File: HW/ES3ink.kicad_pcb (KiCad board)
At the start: 2 copper layers, 60.8 x 30 mm, 79 parts, among them J1 USB_C_Receptacle_USB2.0, J2 Conn_01x24_Pin, J3 Conn_01x02_Pin, J4 Conn_01x04_Socket, J5 USB_C_Receptacle_USB2.0, Q1 DMG3415U-7, Q2 SI1308EDL-T1-GE3, Q3 DMG3415U-7, Q4 SI2305, SW1 RESET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

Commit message: Version 2.5 upload
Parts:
- removed T1, T2, T3, T4: Tab, PCM_kikit:Tab
- removed kibuzzard-64559702: G***, kibuzzard-64559702
- added JP3: SolderJumper_2_Open, Jumper:SolderJumper-2_P1.3mm_Open_TrianglePad1.0x1.5mm, B.Cu at (42.1, -3.23)
- added kibuzzard-65023723: G***, kibuzzard-65023723, B.Cu at (3.00, -15.0)
- L1: value 68uH -> 10uH/1A
- R10: value 10R -> 2R2
- moved G*** 22.0 mm to (13.0, -15.0)
- moved G*** 20.0 mm to (32.5, -15.0)
- moved R3 18.4 mm to (19.2, -27.4), turned to 90 degrees
- moved C7 18.3 mm to (17.2, -27.4), turned to 90 degrees
- moved C22 12.5 mm to (37.9, -12.4), turned to -90 degrees
- moved R11 8.23 mm to (27.6, -12.4), turned to 90 degrees
- moved C13 8.18 mm to (29.7, -12.4), turned to 90 degrees
- moved Q2 7.70 mm to (38.7, -16.8), turned to -90 degrees
- moved C19 6.15 mm to (35.8, -16.9)
- moved L1 5.72 mm to (41.9, -12.6), turned to 0 degrees
- moved C14 4.50 mm to (35.8, -12.4), turned to -90 degrees
- moved R12 4.07 mm to (45.8, -12.4)
- moved D5 3.69 mm to (45.2, -16.9)
- moved Q3 3.60 mm to (42.2, -16.8)
- moved R10 3.46 mm to (41.9, -8.85)
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- renumbered C2 to C12.3546, R9 to R8.8456
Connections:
- Q1 pad 3: Net-(Q1-D) -> /3V3_EPD
- R10 pad 1: Net-(Q1-D) -> Net-(JP3-A)
- R10 pad 2: /3V3_EPD -> GND
- R8.8456 pad 2: GND -> Net-(JP3-A)
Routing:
- net /3V3_EPD: track 50.5 -> 18.9 mm, vias 3 -> 2
- net Net-(Q1-D): track 13.5 -> 0.00 mm
- net Net-(D1-A): track 32.3 -> 19.5 mm, vias 3 -> 0
- net /IO0: track 30.9 -> 20.0 mm, vias 0 -> 2
- net Net-(D5-K): track 77.6 -> 66.8 mm
- net Net-(D2-K): track 15.0 -> 5.21 mm, vias 2 -> 0
- net /GDR: track 15.9 -> 25.6 mm
- net /EN: track 43.4 -> 52.6 mm
- net Net-(JP3-A): track 0.00 -> 7.92 mm, vias 0 -> 1
- net /RESE: track 16.0 -> 23.5 mm
- net /IO48: track 26.4 -> 20.9 mm
- net GND: track 9.72 -> 4.67 mm, vias 20 -> 23
- net /IO8: track 13.7 -> 18.8 mm, vias 0 -> 2
- net /IO18: track 20.1 -> 15.1 mm, vias 2 -> 0
- net /P8: track 16.9 -> 21.6 mm, vias 0 -> 2
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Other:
- board text added: "R2.5"
- board text removed: "rev.Bi4"

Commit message: Layout change & production files
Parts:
- added G***: LOGO, LOGO, B.Cu at (44.3, -15.0)
- moved J4 21.7 mm to (24.5, -27.1)
- moved R6 21.4 mm to (25.7, -21.3)
- moved R7 21.3 mm to (23.7, -21.3)
- moved kibuzzard-64921EFB 19.1 mm to (47.6, -20.7)
- moved J3 19.0 mm to (44.2, -25.1)
- moved kibuzzard-64921EEB 18.9 mm to (40.8, -20.7)
- moved R20 13.3 mm to (29.6, -21.3), turned to -90 degrees
- moved C4 12.7 mm to (27.6, -21.3), turned to -90 degrees
- moved R19 9.38 mm to (31.6, -21.3), turned to -90 degrees
- moved R18 8.97 mm to (29.5, -28.3)
- moved D4 8.66 mm to (36.2, -21.3), turned to 90 degrees
- moved Q4 8.20 mm to (30.6, -24.8), turned to 180 degrees
- moved R15 5.41 mm to (38.5, -21.3)
- moved R17 4.66 mm to (38.5, -28.3)
- moved C5 4.57 mm to (47.8, -16.9), turned to 90 degrees
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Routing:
- net +5V: track 86.6 -> 60.2 mm
- net /IO4: track 65.2 -> 41.8 mm
- net /IO3: track 73.1 -> 49.7 mm
- net /BAT+: track 19.9 -> 35.0 mm, vias 0 -> 3
- net Net-(D4-K): track 2.02 -> 16.4 mm, vias 0 -> 2
- net /IO40: track 35.3 -> 21.0 mm
- net /IO2: track 44.1 -> 30.8 mm
- net +3V3: track 110.1 -> 121.4 mm, vias 5 -> 4
- net Net-(Q4-G): track 6.24 -> 12.8 mm, vias 0 -> 2
- net Net-(JP1-A): track 1.75 -> 5.40 mm
- net /GDR: track 25.6 -> 22.4 mm
- net Net-(JP2-A): track 1.75 -> 4.51 mm
- net GND: track 4.67 -> 6.65 mm, vias 23 -> 29
- net Net-(U3-STAT): track 2.81 -> 4.57 mm
- net /IO48: track 20.9 -> 19.2 mm
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
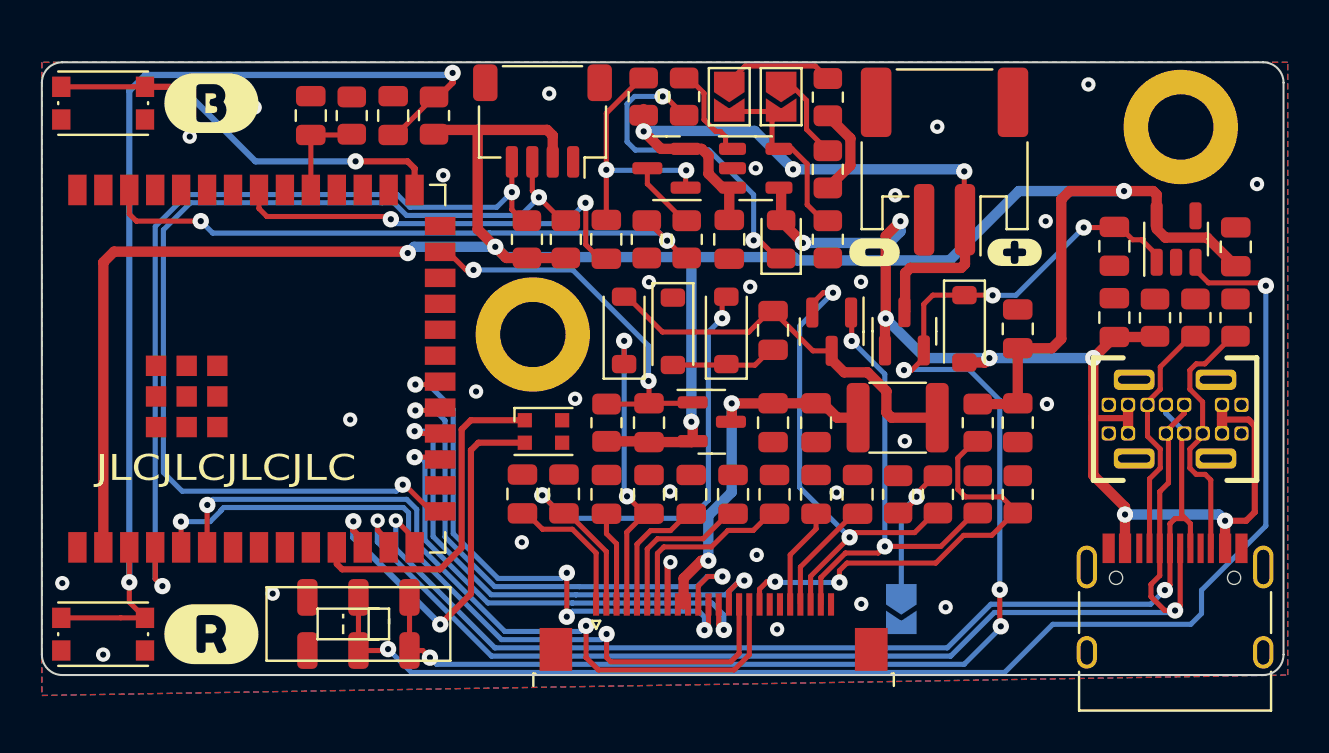
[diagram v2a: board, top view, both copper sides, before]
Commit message: PCB size increase so it can be manufactured with V-cuts
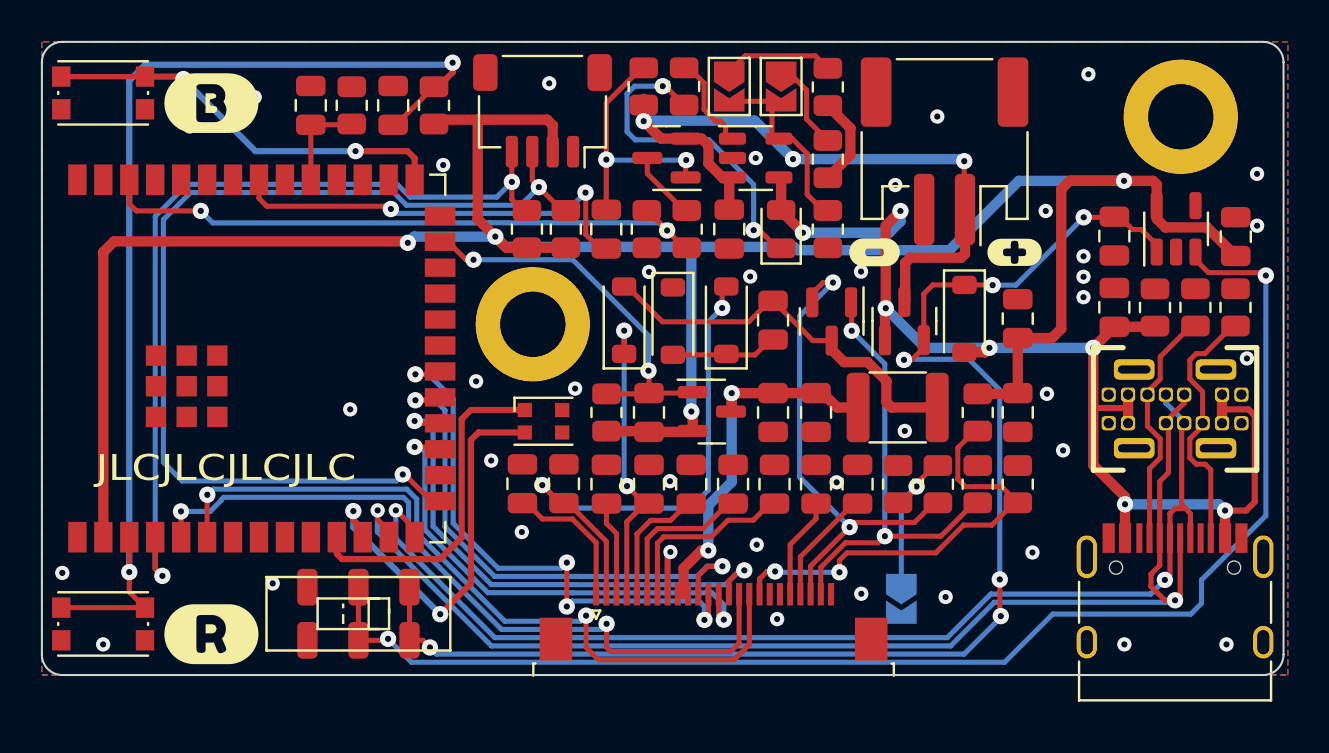
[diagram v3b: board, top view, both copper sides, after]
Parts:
- moved C1 0.50 mm to (52.5, -18.0)
- moved C10 0.50 mm to (23.5, -9.36)
- moved C11 0.50 mm to (33.8, -9.35)
- moved C12 0.50 mm to (35.9, -9.35)
- moved C12.3546 0.50 mm to (47.8, -12.9)
- moved C13 0.50 mm to (29.7, -12.9)
- moved C14 0.50 mm to (35.8, -12.9)
- moved C15 0.50 mm to (37.9, -9.35)
- moved C16 0.50 mm to (39.9, -9.35)
- moved C17 0.50 mm to (29.7, -9.35)
- moved C18 0.50 mm to (31.8, -9.35)
- moved C19 0.50 mm to (35.8, -17.4)
- moved C20 0.50 mm to (33.7, -21.8)
- moved C21 0.50 mm to (52.5, -21.5)
- moved C22 0.50 mm to (37.9, -12.9)
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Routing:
- net GND: vias 29 -> 39
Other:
- board size 60.8 x 30 mm -> 60.8 x 31 mm

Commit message: Update
- pin change to match ESP32-S3 DevKitC 1
- revision change to P1.0 (production)
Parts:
- removed R12: 10K, Resistor_SMD:R_0805_2012Metric
- C4: value 10uF -> 100nF
- Q1: value DMG3415U-7 -> AO3401A
- Q3: value DMG3415U-7 -> DMP2045U-7
- renumbered C12.3546 to C2, R8.8456 to R9
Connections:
- net /P8 renamed /BS
- net Net-(J2-Pin_20) renamed /VGH
- net Net-(J2-Pin_21) renamed /VGL
- C13 pad 2: /IO48 -> /IO46
- D6 pad 1: /IO8 -> /IO14
- D6 pad 4: /IO18 -> /IO48
- J2 pad 12: /IO12 -> /IO13
- J2 pad 13: /IO9 -> /IO10
- J2 pad 14: /IO10 -> /IO7
- J4 pad 3: /IO3 -> /IO9
- J4 pad 4: /IO4 -> /IO8
- Q1 pad 1: /IO48 -> /IO46
- R11 pad 2: /IO48 -> /IO46
- R6 pad 1: /IO3 -> /IO9
- R7 pad 1: /IO4 -> /IO8
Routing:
- net /IO3: track 49.7 -> 0.00 mm, vias 2 -> 0
- net /IO4: track 41.8 -> 0.00 mm, vias 2 -> 0
- net /IO7: track 0.00 -> 31.7 mm, vias 0 -> 4
- net /IO13: track 0.00 -> 27.6 mm, vias 0 -> 2
- net /IO12: track 27.4 -> 0.00 mm, vias 4 -> 0
- net /IO46: track 0.00 -> 16.6 mm, vias 0 -> 2
- net /IO18: track 16.5 -> 0.00 mm
- net /IO48: track 19.2 -> 10.2 mm, vias 2 -> 0
- net /IO14: track 0.00 -> 7.48 mm
- net /IO8: track 20.2 -> 26.9 mm
- net /BS: track 21.6 -> 15.3 mm
- net /IO11: track 25.7 -> 23.2 mm
- net +3V3: track 121.4 -> 119.5 mm
- net /IO10: track 25.5 -> 24.2 mm
- net GND: track 6.65 -> 5.60 mm
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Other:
- board text added: "P1.0"
- board text removed: "R2.5"

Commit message: R18 value change
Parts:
- R18: value 10K -> 1M
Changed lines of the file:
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@@
         (effects (font (size 1 1) (thickness 0.15)))
     )
-    (fp_text value "10K" (at 0 1.65 90) (layer "F.Fab") hide
+    (fp_text value "1M" (at 0 1.65 90) (layer "F.Fab") hide
         (effects (font (size 1 1) (thickness 0.15)))
     )

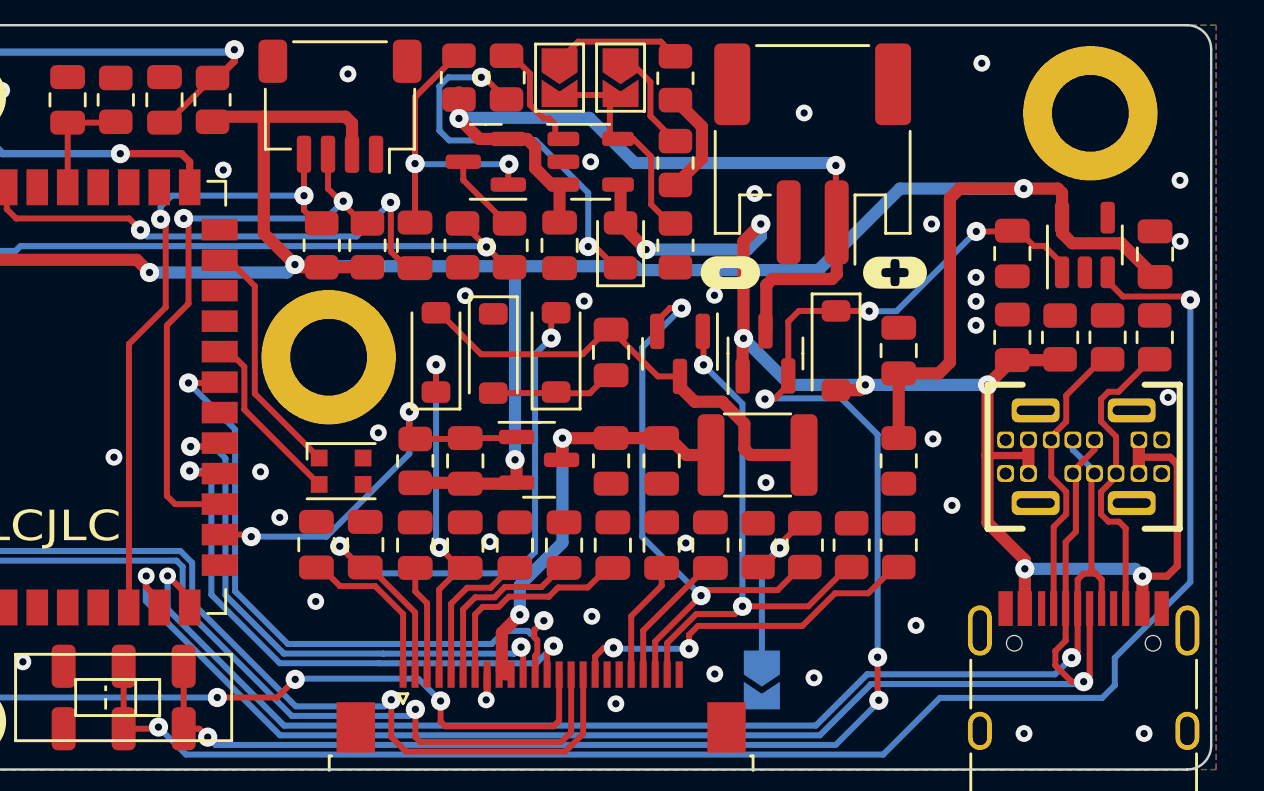
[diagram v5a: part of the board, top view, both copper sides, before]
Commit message: Update
- fix I2C pin at Qwiic connector
- fix SPI CLK pin for EPD
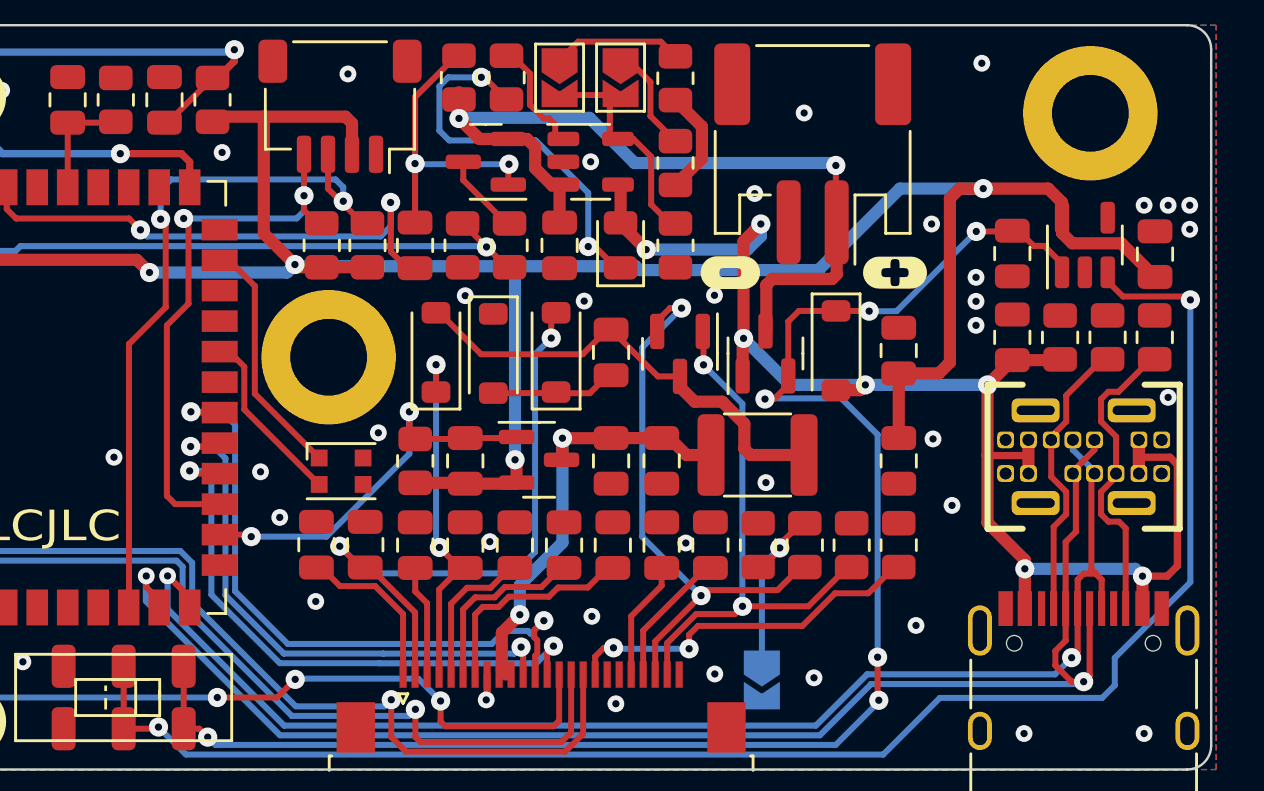
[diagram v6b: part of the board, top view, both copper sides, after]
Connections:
- J2 pad 12: /IO13 -> /IO12
- J4 pad 3: /IO9 -> /IO8
- J4 pad 4: /IO8 -> /IO9
- R6 pad 1: /IO9 -> /IO8
- R7 pad 1: /IO8 -> /IO9
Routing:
- net /IO13: track 27.6 -> 0.05 mm, vias 2 -> 0
- net /IO12: track 0.00 -> 27.0 mm, vias 0 -> 2
- net /IO8: track 26.9 -> 30.3 mm
- net +3V3: track 119.5 -> 117.5 mm
- net /IO9: track 25.0 -> 23.4 mm
- net /IO40: track 21.3 -> 21.9 mm
- net GND: vias 39 -> 41

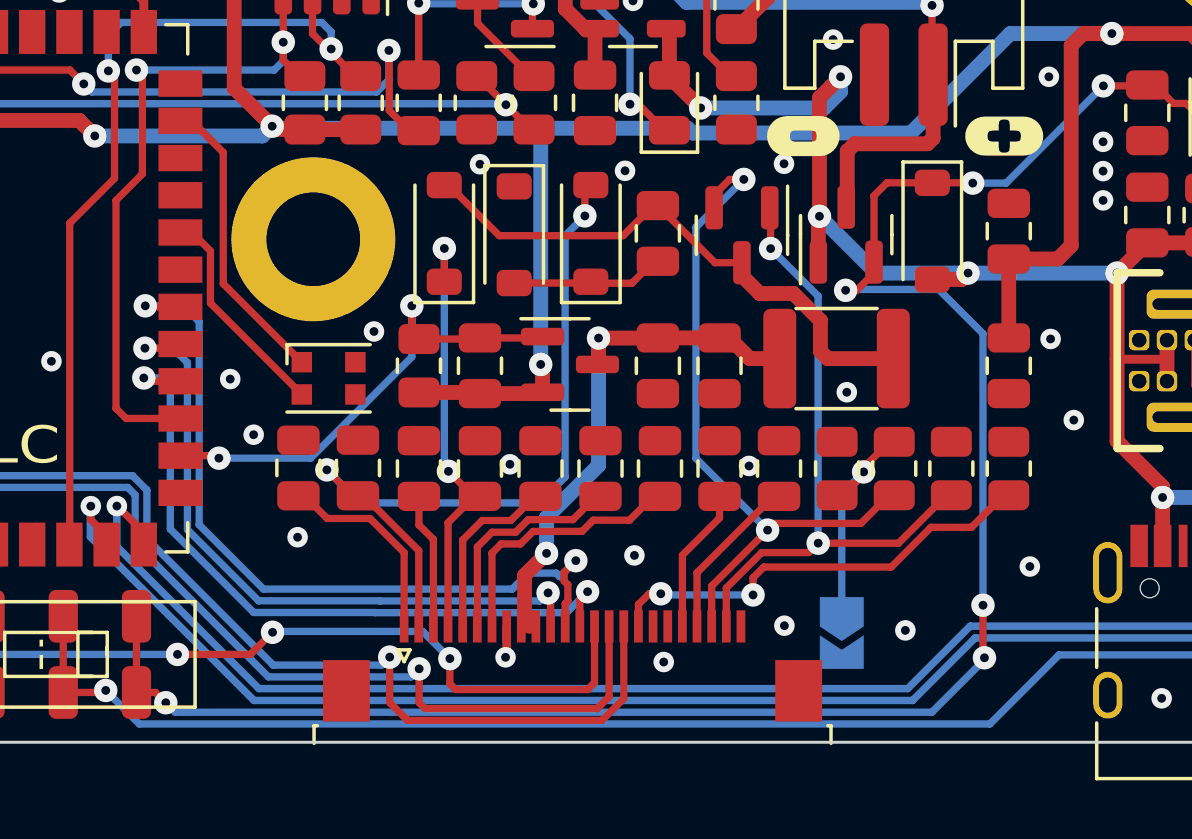
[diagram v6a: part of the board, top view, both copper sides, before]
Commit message: Update
- component value change
- FPC connector changed to double side connection
- version increase to 1.1
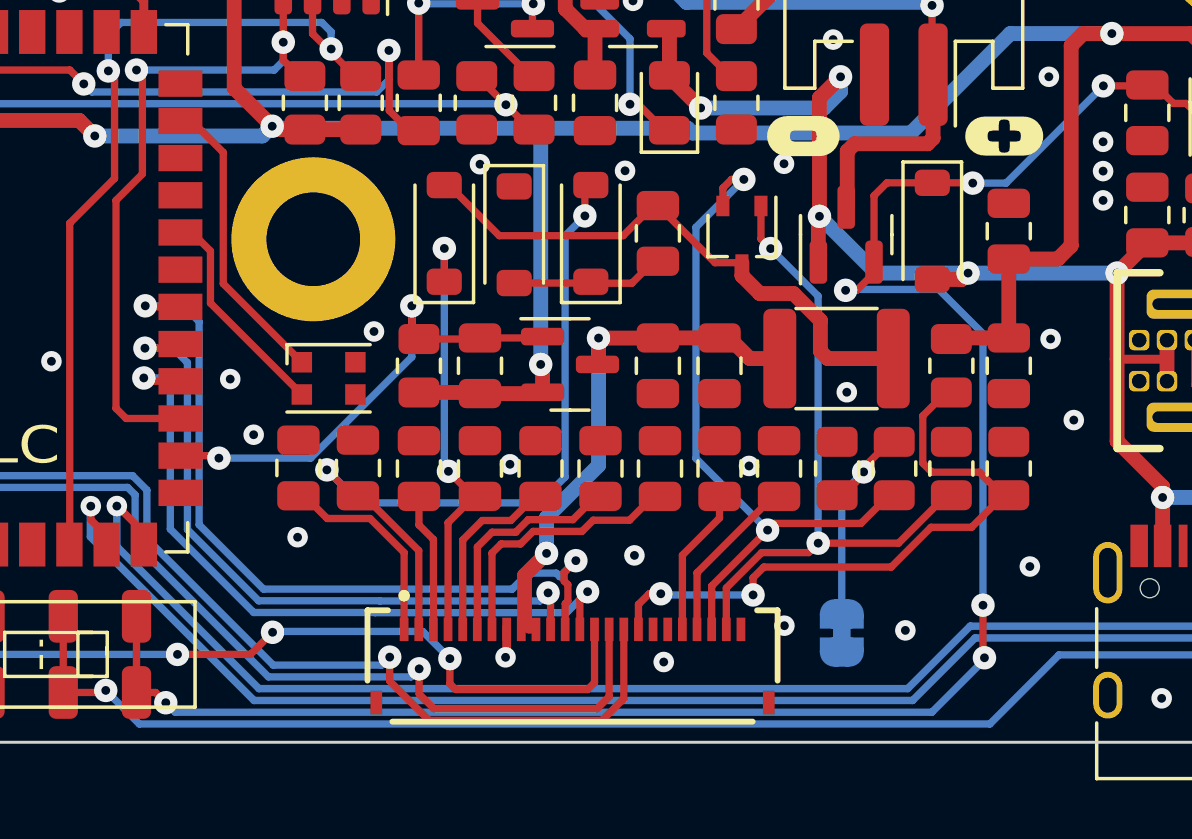
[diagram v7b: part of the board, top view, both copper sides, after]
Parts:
- removed kibuzzard-65023723: G***, kibuzzard-65023723
- added R12: 10K, Resistor_SMD:R_0805_2012Metric, F.Cu at (45.8, -12.9)
- added kibuzzard-65272A96: G***, kibuzzard-65272A96, B.Cu at (3.00, -15.0)
- D1, D2, D3: value MBR0520LT -> MBR0530
- J2: footprint Connector_FFC-FPC:TE_2-1734839-4_1x24-1MP_P0.5mm_Horizontal -> dronecz:GCT_FFC2B28-24-G
- JP3: footprint Jumper:SolderJumper-2_P1.3mm_Open_TrianglePad1.0x1.5mm -> Jumper:SolderJumper-2_P1.3mm_Bridged_RoundedPad1.0x1.5mm
- Q2: footprint Package_TO_SOT_SMD:SOT-23 -> Package_TO_SOT_SMD:SOT-323_SC-70
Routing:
- net /BS: track 15.3 -> 21.6 mm
- net +3V3: track 117.5 -> 119.5 mm
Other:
- board text added: "P1.1"
- board text removed: "P1.0"
